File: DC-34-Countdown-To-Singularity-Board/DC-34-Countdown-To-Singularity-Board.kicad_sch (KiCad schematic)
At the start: 54 parts, among them J1 DCJ200-10-A-XX-K_REVA, J10 Conn_01x06_Male, J2 Conn_01x05_Male, J3 Conn_01x06_Male, J4 Conn_01x06_Male, J5 Conn_01x06_Male, J6 Conn_01x06_Male, J7 Conn_01x06_Male, J8 Conn_01x06_Male, J9 Conn_01x06_Male, SW1 SW_DIP_x01, SW2 SW_DIP_x01, SW3 SW_DIP_x01, U1 LM7805_TO220, U2 LM317_TO-220, U3 ATmega328P-P, U4 PCF8523T, U5 CC56-12CGKWA, U6 CC56-12CGKWA, X1 SG-3030CM, Y1 Crystal

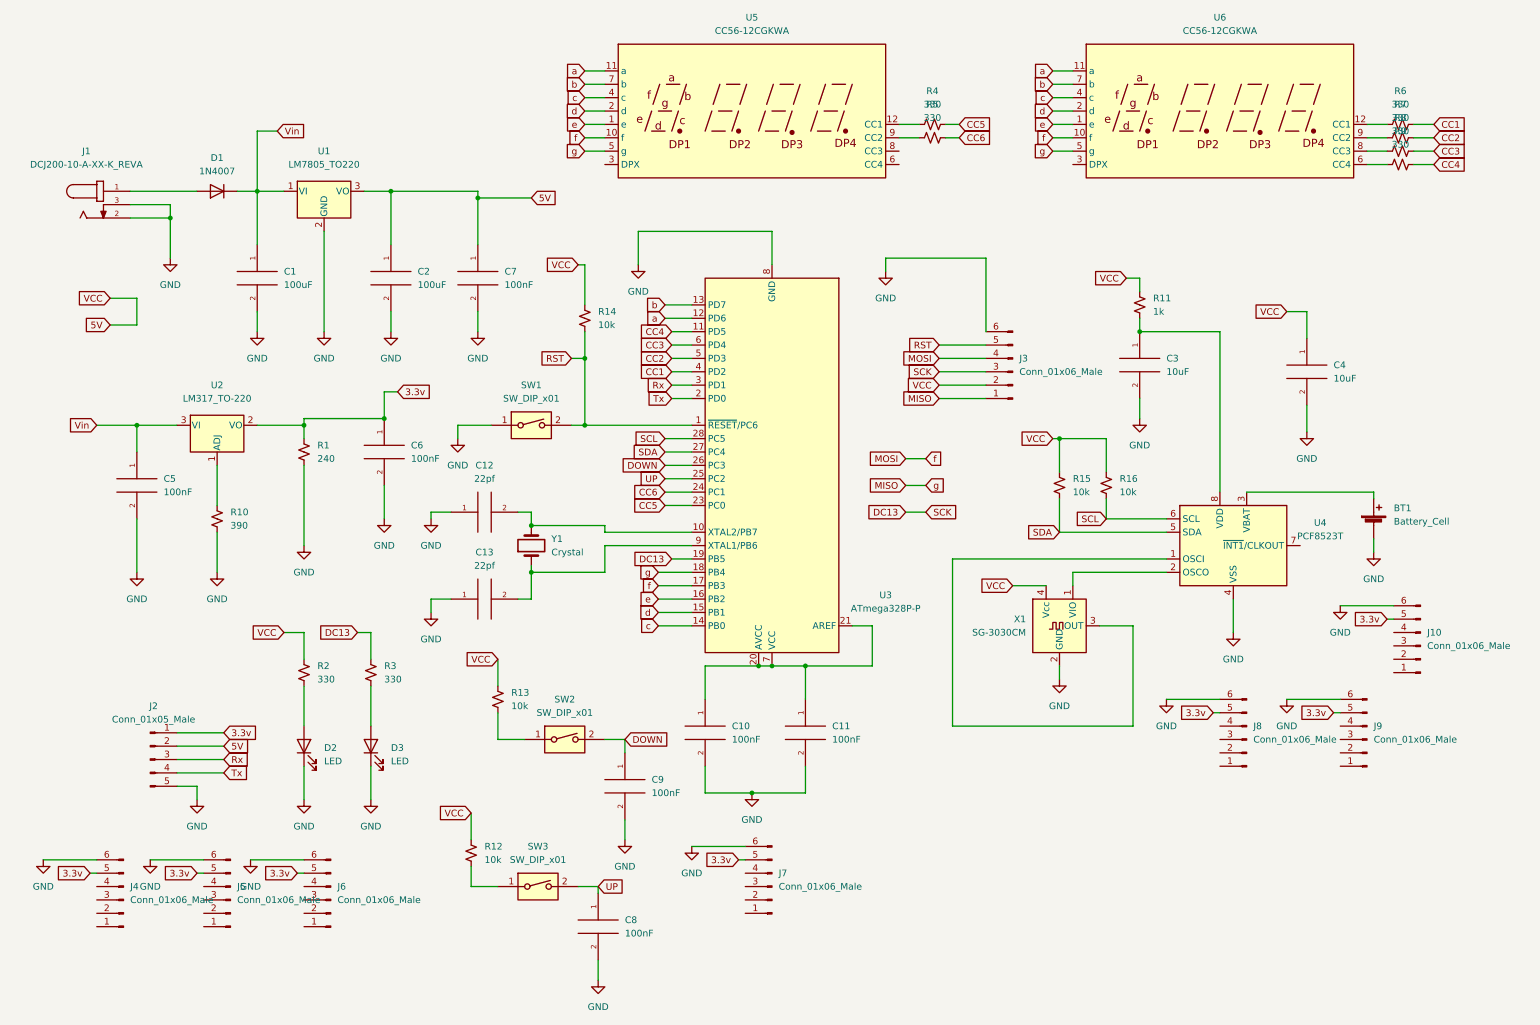
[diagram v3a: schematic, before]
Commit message: Updated Crystal information and circuit for Real-time clock.
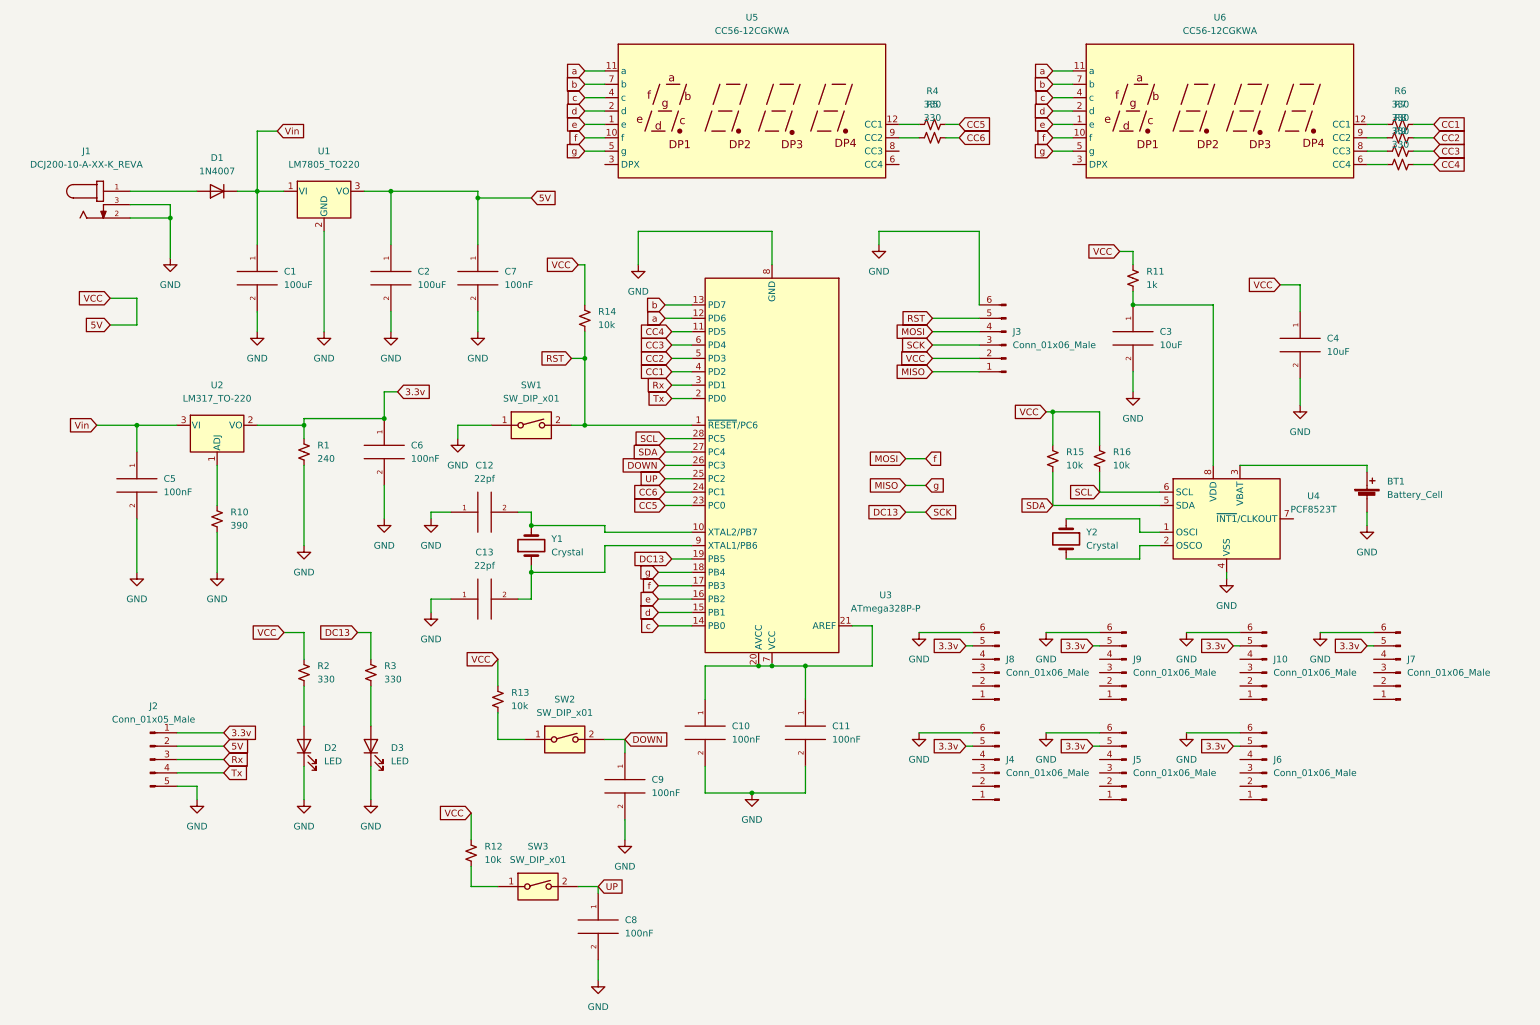
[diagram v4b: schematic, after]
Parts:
- removed X1: SG-3030CM, Oscillator:Oscillator_SMD_SeikoEpson_SG3030CM, symbol Oscillator:SG-3030CM
- added Y2: Crystal, Crystal:Crystal_SMD_SeikoEpson_MC306-4Pin_8.0x3.2mm, symbol Device:Crystal
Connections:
- net at U4.2 (OSCO): now also Y2.2
- net at U4.1 (OSCI): now also Y2.1
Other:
- moved on the sheet: BT1, C3, C4, J10, J3, J4, J5, J6, J7, J8, J9, R11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

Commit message: Made Bootloader programmer use 10-pin adaptor.
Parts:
- removed J3: Conn_01x06_Male, Connector_PinHeader_2.54mm:PinHeader_2x03_P2.54mm_Vertical, symbol Connector:Conn_01x06_Male
- added J3: Conn_01x10_Male, Connector_PinSocket_2.54mm:PinSocket_2x05_P2.54mm_Vertical, symbol Connector:Conn_01x10_Male
- R12, R13: value 10k -> 1k
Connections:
- net 5V: now also J2.5 (Pin_5), J3.2 (Pin_2); no longer J2.2 (Pin_2), R12.1, R13.1
- net DC13: now also J3.7 (Pin_7)
- net GND: now also J2.4 (Pin_4), R12.2, R13.2, J3.10 (Pin_10), J3.8 (Pin_8); no longer J2.5 (Pin_5)
- net MISO: now also J3.9 (Pin_9)
- net MOSI: now also J3.1 (Pin_1)
- net RST: now also J3.5 (Pin_5)
- net Tx: now also J2.2 (Pin_2); no longer J2.4 (Pin_4)
- net at SW2.1: now also R13.1; no longer R13.2
- net at SW3.1: now also R12.1; no longer R12.2
- no-connect marks 0 -> 36
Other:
- moved on the sheet: C8, C9, R12, R13, SW2, SW3

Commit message: Final submission to PCBWay.
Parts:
- C10, C11, C12, C13, C5, C6, C7, C8, C9: footprint Capacitor_THT:C_Radial_D10.0mm_H12.5mm_P5.00mm -> Capacitor_THT:C_Rect_L7.0mm_W3.5mm_P5.00mm
- R1, R10, R11, R12, R13, R14, R15, R16, R2, R3, R4, R5, R6, R7, R8, R9: footprint Resistor_THT:R_Axial_DIN0207_L6.3mm_D2.5mm_P2.54mm_Vertical -> Resistor_THT:R_Axial_DIN0207_L6.3mm_D2.5mm_P15.24mm_Horizontal
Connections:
- net 5V: now also C10.1, C11.1, U3.20 (AVCC), U3.21 (AREF), U3.7 (VCC)
